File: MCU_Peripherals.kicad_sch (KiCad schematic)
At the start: 17 parts

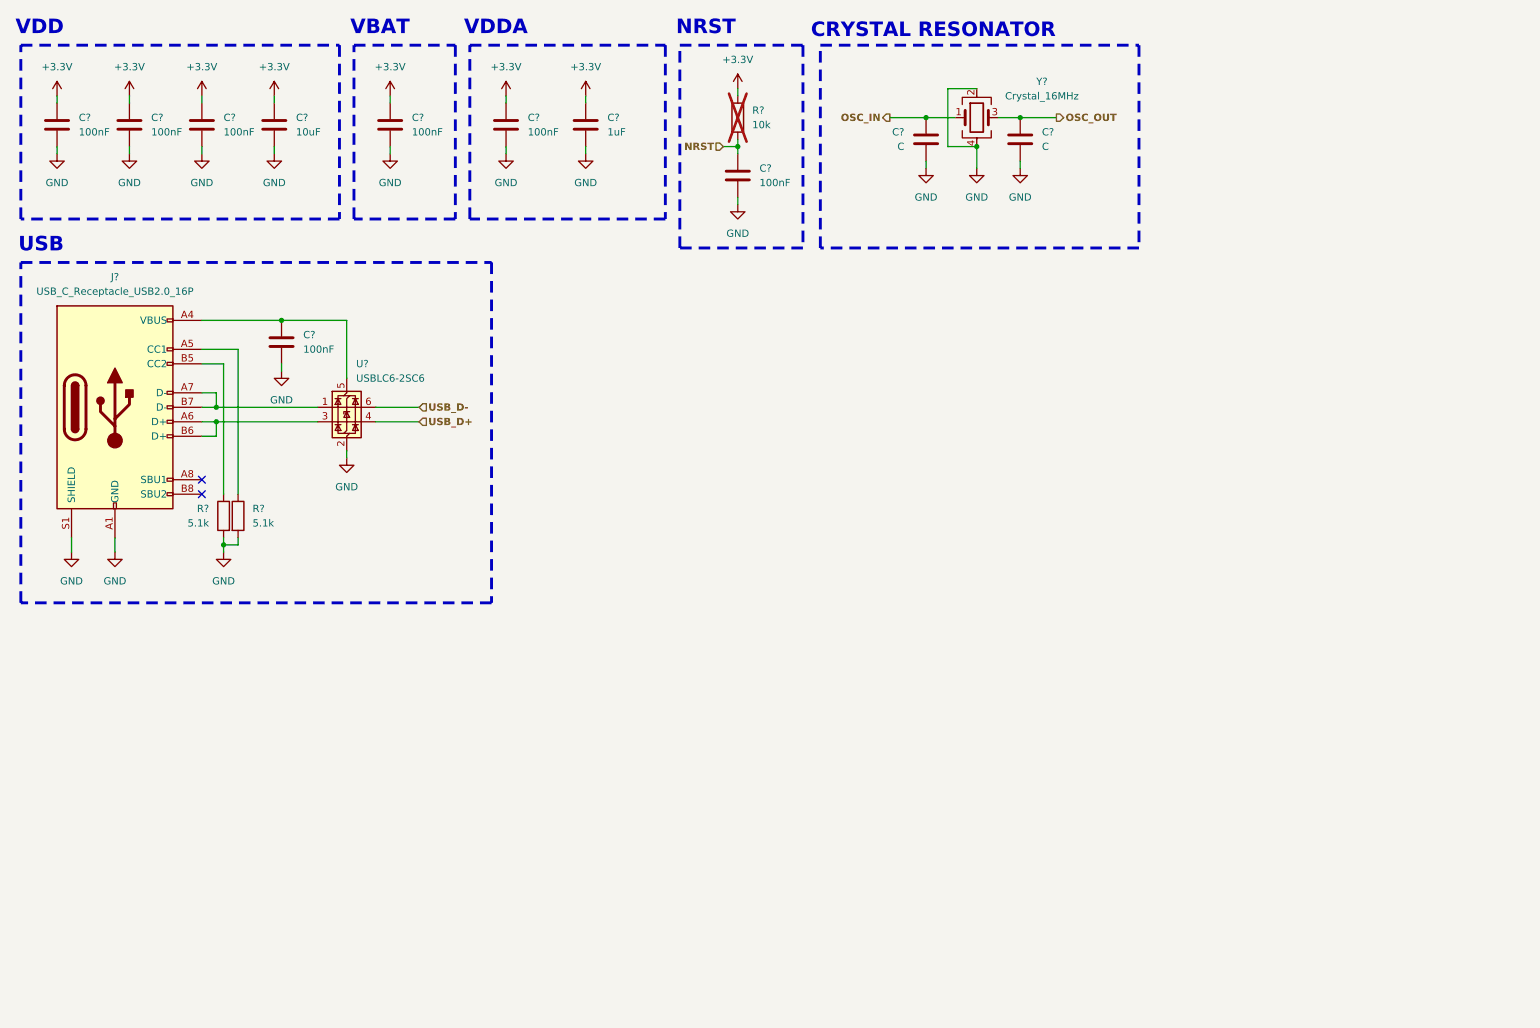
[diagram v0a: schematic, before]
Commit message: Power Rail Update
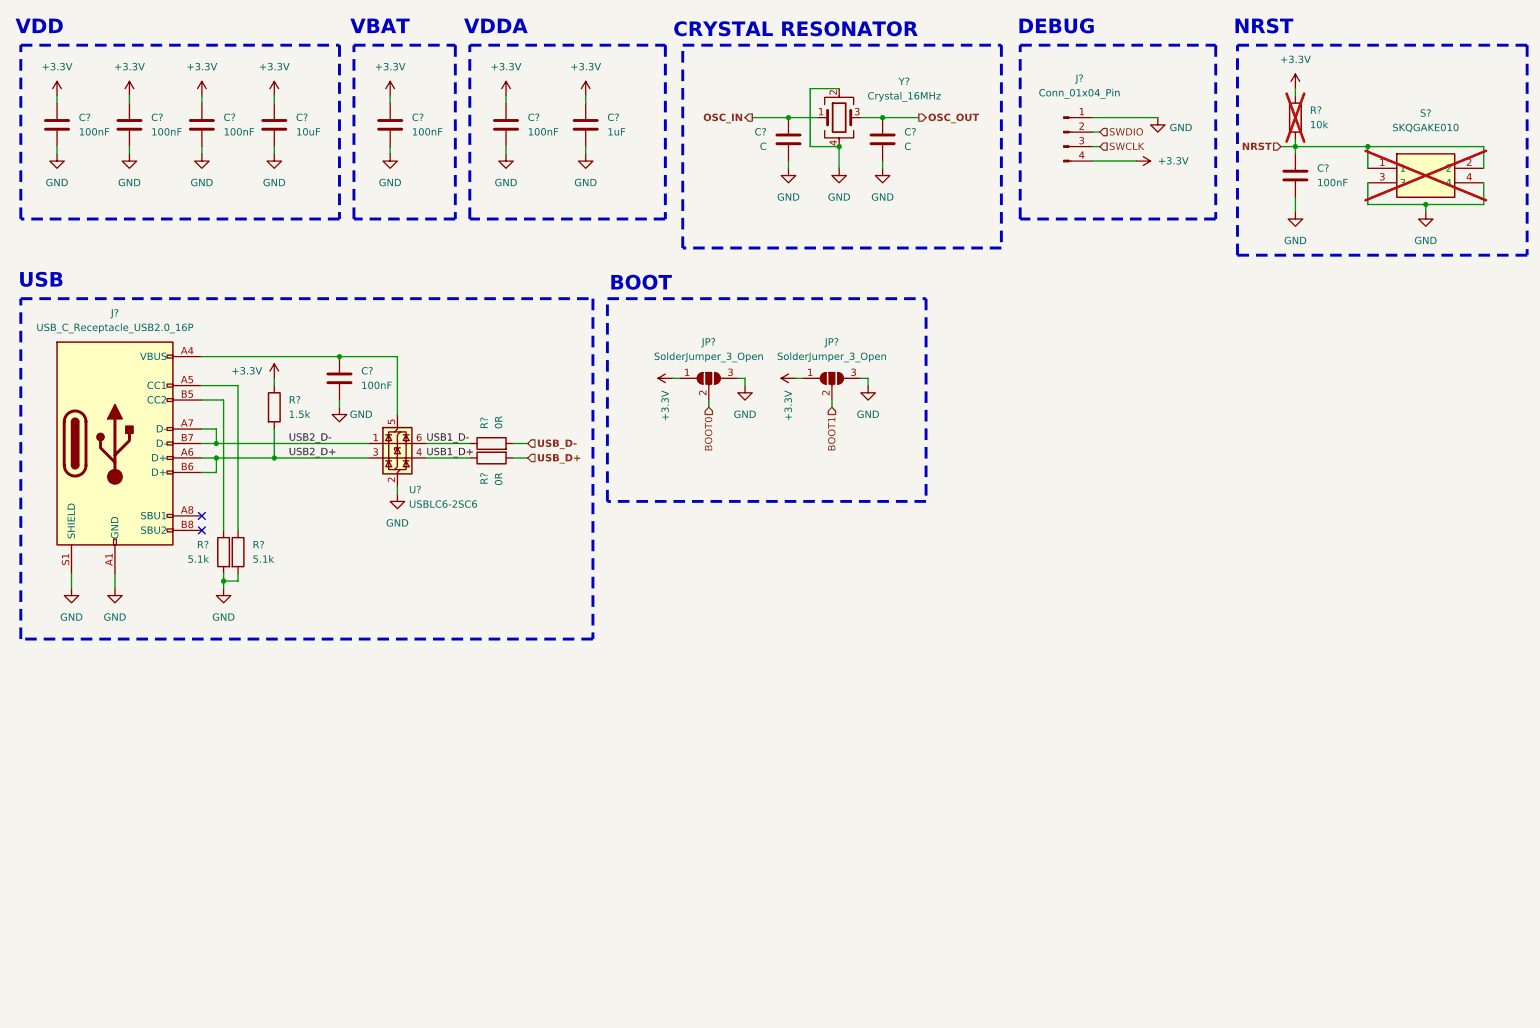
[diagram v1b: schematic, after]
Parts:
- added J?: Conn_01x04_Pin, symbol Connector:Conn_01x04_Pin
- added JP? (x2): SolderJumper_3_Open, symbol Jumper:SolderJumper_3_Open
- added R? (x2): 0R, symbol Device:R
- added R?: 1.5k, symbol Device:R
- added S?: SKQGAKE010, KSZ_KiCad_Footprint_Library:SKQGAKE010, symbol KSZ_KiCad_Symbol_Library:SKQGAKE010
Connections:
- net +3.3V: now also J?.4 (Pin_4), JP?.1 (A), JP?.1 (A), R?.1
- net GND: now also J?.1 (Pin_1), JP?.3 (B), JP?.3 (B), S?.3, S?.4
- net NRST: now also S?.1, S?.2
- net USB_D+: now also R?.2; no longer U?.4 (I/O2)
- net USB_D-: now also R?.2; no longer U?.6 (I/O1)
- net USB2_D+: now reaches J?.A6 (D+), J?.B6 (D+), U?.3 (I/O2)
- net USB2_D+: now also R?.2
- net USB2_D-: now reaches J?.A7 (D-), J?.B7 (D-), U?.1 (I/O1)
- new net BOOT0: JP?.2 (C)
- new net BOOT1: JP?.2 (C)
- new net SWCLK: J?.3 (Pin_3)
- new net SWDIO: J?.2 (Pin_2)
- new net USB1_D+: R?.1, U?.4 (I/O2)
- new net USB1_D-: R?.1, U?.6 (I/O1)
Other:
- note added: "BOOT"
- note added: "DEBUG"
- moved on the sheet: C?, J?, R?, U?, Y?

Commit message: Stepper Motor Control Update
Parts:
- added R? (x2): 4.7k, symbol Device:R
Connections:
- net +3.3V: now also R?.1, R?.1
- new net SCL: R?.2
- new net SDA: R?.2
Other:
- note added: "I2C"

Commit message: CAN & EEPROM Update
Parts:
- added C? (x2): 100nF, symbol Device:C
- added D?: PESD2CANFD24V-UX, KSZ_KiCad_Footprint_Library:TVS_PESD2CANFD24V-UX, symbol KSZ_KiCad_Symbol_Library:PESD2CANFD24V-UX
- added J?: Conn_01x02_Socket, symbol Connector:Conn_01x02_Socket
- added JP? (x3): SolderJumper_3_Open, symbol Jumper:SolderJumper_3_Open
- added R?: 120R, symbol Device:R
- added R?: 10k, symbol Device:R
- added U?: SN65HVD230DR, KSZ_KiCad_Footprint_Library:SOIC127P599X175-8N, symbol KSZ_KiCad_Symbol_Library:SN65HVD230DR
- added U?: M24C64-RMN6TP, KSZ_KiCad_Footprint_Library:SOIC127P600X175-8N, symbol KSZ_KiCad_Symbol_Library:M24C64-RMN6TP
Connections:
- net +3.3V: now also C?.1, C?.1, JP?.1 (A), JP?.1 (A), JP?.1 (A), U?.3 (VCC), U?.8 (VCC)
- net GND: now also C?.2, C?.2, D?.3, JP?.3 (B), JP?.3 (B), JP?.3 (B), R?.2, U?.2 (GND), U?.4 (VSS)
- new net: D?.1, J?.2 (Pin_2), R?.2, U?.6 (CANL)
- new net: D?.2, J?.1 (Pin_1), R?.1, U?.7 (CANH)
- new net: R?.1, U?.8 (RS)
- new net CAN_RX: U?.4 (R)
- new net CAN_TX: U?.1 (D)
- new net E0: JP?.2 (C), U?.1 (E0)
- new net E1: JP?.2 (C), U?.2 (E1)
- new net E2: JP?.2 (C), U?.3 (E2)
- new net SCL_EEPROM: U?.6 (SCL)
- new net SDA_EEPROM: U?.5 (SDA)
- new net WC_EEPROM: U?.7 (~{WC})
- no-connect marks 2 -> 3
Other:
- note added: "CAN"
- note added: "EEPROM"

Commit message: LEDs, Button & Small fixes
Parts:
- added D?: R_LED, symbol Device:LED
- added D?: B_LED, symbol Device:LED
- added D?: G_LED, symbol Device:LED
- added R? (x3): 1.5k, symbol Device:R
- added R?: 10k, symbol Device:R
- added S?: SKQGAKE010, KSZ_KiCad_Footprint_Library:SKQGAKE010, symbol KSZ_KiCad_Symbol_Library:SKQGAKE010
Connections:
- net +3.3V: now also D?.2 (A), D?.2 (A), D?.2 (A), R?.1
- net GND: now also S?.3, S?.4
- new net: D?.1 (K), R?.1 (x3)
- new net B_LED: R?.2
- new net G_LED: R?.2
- new net R_LED: R?.2
- new net U_BUTTON: R?.2, S?.1, S?.2
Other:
- note added: "STATE_LEDS"
- note added: "USER_BUTTON"

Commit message: Schematic finish & ERC
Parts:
- gave numbers to parts that had none: 45

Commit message: Footprint Update
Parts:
- C1, C10, C11, C12, C13, C2, C3, C4, C5, C6, C7, C8, C9: footprint (none) -> Capacitor_SMD:C_0402_1005Metric_Pad0.74x0.62mm_HandSolder
- D2, D3, D4: footprint (none) -> LED_SMD:LED_0603_1608Metric_Pad1.05x0.95mm_HandSolder
- J1: footprint (none) -> Connector_USB:USB_C_Receptacle_HRO_TYPE-C-31-M-12
- J2: footprint (none) -> TerminalBlock:TerminalBlock_MaiXu_MX126-5.0-02P_1x02_P5.00mm
- J3: footprint (none) -> Connector_PinHeader_2.54mm:PinHeader_1x04_P2.54mm_Vertical
- JP1, JP2, JP3, JP4, JP5: footprint (none) -> Jumper:SolderJumper-3_P1.3mm_Open_RoundedPad1.0x1.5mm_NumberLabels
- R1, R10, R11, R12, R13, R14, R2, R3, R4, R5, R6, R7, R8, R9: footprint (none) -> Resistor_SMD:R_0402_1005Metric_Pad0.72x0.64mm_HandSolder
- Y1: footprint (none) -> Crystal:Crystal_SMD_3225-4Pin_3.2x2.5mm_HandSoldering
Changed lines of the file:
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@@
 			)
 		)
-		(property "Footprint" ""
+		(property "Footprint" "Jumper:SolderJumper-3_P1.3mm_Open_RoundedPad1.0x1.5mm_NumberLabels"
 			(at 208.28 115.57 0)
 			(effects
@@
 			)
 		)
-		(property "Footprint" ""
+		(property "Footprint" "Capacitor_SMD:C_0402_1005Metric_Pad0.74x0.62mm_HandSolder"
 			(at 72.0852 81.28 0)
 			(effects
@@
 			)
 		)
-		(property "Footprint" ""
+		(property "Footprint" "Resistor_SMD:R_0402_1005Metric_Pad0.72x0.64mm_HandSolder"
 			(at 51.562 107.95 90)
 			(effects
@@
 			)
 		)
-		(property "Footprint" ""
+		(property "Footprint" "Capacitor_SMD:C_0402_1005Metric_Pad0.74x0.62mm_HandSolder"
 			(at 167.3352 39.37 0)
 			(effects
@@
 			)
 		)
-		(property "Footprint" ""
+		(property "Footprint" "Capacitor_SMD:C_0402_1005Metric_Pad0.74x0.62mm_HandSolder"
 			(at 115.2652 36.83 0)
 			(effects
@@
 			)
 		)
-		(property "Footprint" ""
+		(property "Footprint" "Resistor_SMD:R_0402_1005Metric_Pad0.72x0.64mm_HandSolder"
 			(at 97.79 89.662 90)
 			(effects
@@
 			)
 		)
-		(property "Footprint" ""
+		(property "Footprint" "LED_SMD:LED_0603_1608Metric_Pad1.05x0.95mm_HandSolder"
 			(at 128.27 163.83 0)
 			(effects
@@
 			)
 		)
-		(property "Footprint" ""
+		(property "Footprint" "Jumper:SolderJumper-3_P1.3mm_Open_RoundedPad1.0x1.5mm_NumberLabels"
 			(at 208.28 129.54 0)
 			(effects
@@
 			)
 		)
-		(property "Footprint" ""
+		(property "Footprint" "Jumper:SolderJumper-3_P1.3mm_Open_RoundedPad1.0x1.5mm_NumberLabels"
 			(at 135.89 77.47 0)
 			(effects
@@
 			)
 		)
-		(property "Footprint" ""
+		(property "Footprint" "Capacitor_SMD:C_0402_1005Metric_Pad0.74x0.62mm_HandSolder"
 			(at 47.9552 36.83 0)
 			(effects
@@
 			)
 		)
-		(property "Footprint" ""
+		(property "Footprint" "Resistor_SMD:R_0402_1005Metric_Pad0.72x0.64mm_HandSolder"
 			(at 52.578 107.95 90)
 			(effects
@@
 			)
 		)
-		(property "Footprint" ""
+		(property "Footprint" "Capacitor_SMD:C_0402_1005Metric_Pad0.74x0.62mm_HandSolder"
 			(at 101.2952 36.83 0)
 			(effects
@@
 			)
 		)
-		(property "Footprint" ""
+		(property "Footprint" "Jumper:SolderJumper-3_P1.3mm_Open_RoundedPad1.0x1.5mm_NumberLabels"
 			(at 241.3 115.57 0)
 			(effects
@@
 			)
 		)
-		(property "Footprint" ""
+		(property "Footprint" "LED_SMD:LED_0603_1608Metric_Pad1.05x0.95mm_HandSolder"
 			(at 139.7 163.83 0)
 			(effects
@@
 			)
 		)
-		(property "Footprint" ""
+		(property "Footprint" "Connector_PinHeader_2.54mm:PinHeader_1x04_P2.54mm_Vertical"
 			(at 198.12 34.29 0)
 			(effects
@@
 			)
 		)
-		(property "Footprint" ""
+		(property "Footprint" "Resistor_SMD:R_0402_1005Metric_Pad0.72x0.64mm_HandSolder"
 			(at 195.072 74.93 90)
 			(effects
@@
 			)
 		)
-		(property "Footprint" ""
+		(property "Footprint" "Capacitor_SMD:C_0402_1005Metric_Pad0.74x0.62mm_HandSolder"
 			(at 239.7252 45.72 0)
 			(effects
@@
 			)
 		)
-		(property "Footprint" ""
+		(property "Footprint" "Resistor_SMD:R_0402_1005Metric_Pad0.72x0.64mm_HandSolder"
 			(at 83.312 149.86 90)
 			(effects
@@
 			)
 		)
-		(property "Footprint" ""
+		(property "Footprint" "Jumper:SolderJumper-3_P1.3mm_Open_RoundedPad1.0x1.5mm_NumberLabels"
 			(at 157.48 77.47 0)
 			(effects
@@
 			)
 		)
-		(property "Footprint" ""
+		(property "Footprint" "Resistor_SMD:R_0402_1005Metric_Pad0.72x0.64mm_HandSolder"
 			(at 57.912 82.55 90)
 			(effects
@@
 			)
 		)
-		(property "Footprint" ""
+		(property "Footprint" "Connector_USB:USB_C_Receptacle_HRO_TYPE-C-31-M-12"
 			(at 35.56 88.9 0)
 			(effects
@@
 			)
 		)
-		(property "Footprint" ""
+		(property "Footprint" "Resistor_SMD:R_0402_1005Metric_Pad0.72x0.64mm_HandSolder"
 			(at 203.962 74.93 90)
 			(effects
@@
 			)
 		)
-		(property "Footprint" ""
+		(property "Footprint" "Capacitor_SMD:C_0402_1005Metric_Pad0.74x0.62mm_HandSolder"
 			(at 177.8 117.1448 0)
 			(effects
@@
 			)
 		)
-		(property "Footprint" ""
+		(property "Footprint" "Resistor_SMD:R_0402_1005Metric_Pad0.72x0.64mm_HandSolder"
 			(at 97.79 90.678 90)
 			(effects
@@
 			)
 		)
-		(property "Footprint" ""
+		(property "Footprint" "Capacitor_SMD:C_0402_1005Metric_Pad0.74x0.62mm_HandSolder"
 			(at 60.6552 36.83 0)
 			(effects
@@
 			)
 		)
-		(property "Footprint" ""
+		(property "Footprint" "Resistor_SMD:R_0402_1005Metric_Pad0.72x0.64mm_HandSolder"
 			(at 130.048 172.72 90)
 			(effects
@@
 			)
 		)
-		(property "Footprint" ""
+		(property "Footprint" "Capacitor_SMD:C_0402_1005Metric_Pad0.74x0.62mm_HandSolder"
 			(at 148.8948 39.37 0)
 			(effects
@@
 			)
 		)
-		(property "Footprint" ""
+		(property "Footprint" "Resistor_SMD:R_0402_1005Metric_Pad0.72x0.64mm_HandSolder"
 			(at 236.982 76.2 90)
 			(effects
@@
 			)
 		)
-		(property "Footprint" ""
+		(property "Footprint" "Resistor_SMD:R_0402_1005Metric_Pad0.72x0.64mm_HandSolder"
 			(at 141.478 172.72 90)
 			(effects
@@
 			)
 		)
-		(property "Footprint" ""
+		(property "Footprint" "Capacitor_SMD:C_0402_1005Metric_Pad0.74x0.62mm_HandSolder"
 			(at 22.5552 36.83 0)
 			(effects
@@
 			)
 		)
-		(property "Footprint" ""
+		(property "Footprint" "LED_SMD:LED_0603_1608Metric_Pad1.05x0.95mm_HandSolder"
 			(at 151.13 163.83 0)
 			(effects
@@
 			)
 		)
-		(property "Footprint" ""
+		(property "Footprint" "Capacitor_SMD:C_0402_1005Metric_Pad0.74x0.62mm_HandSolder"
 			(at 35.2552 36.83 0)
 			(effects
@@
 			)
 		)
-		(property "Footprint" ""
+		(property "Footprint" "TerminalBlock:TerminalBlock_MaiXu_MX126-5.0-02P_1x02_P5.00mm"
 			(at 104.14 148.59 0)
 			(effects
@@
 			)
 		)
-		(property "Footprint" ""
+		(property "Footprint" "Resistor_SMD:R_0402_1005Metric_Pad0.72x0.64mm_HandSolder"
 			(at 30.988 156.21 90)
 			(effects
@@
 			)
 		)
-		(property "Footprint" ""
+		(property "Footprint" "Capacitor_SMD:C_0402_1005Metric_Pad0.74x0.62mm_HandSolder"
 			(at 80.9752 36.83 0)
 			(effects
@@
 			)
 		)
-		(property "Footprint" ""
+		(property "Footprint" "Resistor_SMD:R_0402_1005Metric_Pad0.72x0.64mm_HandSolder"
 			(at 236.982 31.75 90)
 			(effects
@@
 			)
 		)
-		(property "Footprint" ""
+		(property "Footprint" "Resistor_SMD:R_0402_1005Metric_Pad0.72x0.64mm_HandSolder"
 			(at 152.908 172.72 90)
 			(effects
@@
 			)
 		)
-		(property "Footprint" ""
+		(property "Footprint" "Capacitor_SMD:C_0402_1005Metric_Pad0.74x0.62mm_HandSolder"
 			(at 78.74 142.5448 0)
 			(effects
@@
 			)
 		)
-		(property "Footprint" ""
+		(property "Footprint" "Crystal:Crystal_SMD_3225-4Pin_3.2x2.5mm_HandSoldering"
 			(at 158.75 31.75 0)
 			(effects

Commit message: Layout Update
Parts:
- removed C4: 10uF, Capacitor_SMD:C_0402_1005Metric_Pad0.74x0.62mm_HandSolder, symbol Device:C
- removed JP1, JP2, JP3, JP4, JP5: SolderJumper_3_Open, Jumper:SolderJumper-3_P1.3mm_Open_RoundedPad1.0x1.5mm_NumberLabels, symbol Jumper:SolderJumper_3_Open
- removed R13: 10k, Resistor_SMD:R_0402_1005Metric_Pad0.72x0.64mm_HandSolder, symbol Device:R
- removed R6, R7: 0R, Resistor_SMD:R_0402_1005Metric_Pad0.72x0.64mm_HandSolder, symbol Device:R
- removed S1, S2: SKQGAKE010, KSZ_KiCad_Footprint_Library:SKQGAKE010, symbol KSZ_KiCad_Symbol_Library:SKQGAKE010
- added J6: Conn_01x02_Socket, Connector_JST:JST_PH_S2B-PH-K_1x02_P2.00mm_Horizontal, symbol Connector:Conn_01x02_Socket
- added S1: SKRPABE010, KSZ_KiCad_Footprint_Library:SW_SKRPABE010, symbol KSZ_KiCad_Symbol_Library:SKRPABE010
- J2: footprint TerminalBlock:TerminalBlock_MaiXu_MX126-5.0-02P_1x02_P5.00mm -> Connector_JST:JST_PH_S2B-PH-K_1x02_P2.00mm_Horizontal
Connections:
- net E0 is gone; now on net GND: U4.1 (E0)
- net E1 is gone; now on net GND: U4.2 (E1)
- net E2 is gone; now on net GND: U4.3 (E2)
- net USB1_D+ is gone; now on net USB_D+: U3.4 (I/O2)
- net USB1_D- is gone; now on net USB_D-: U3.6 (I/O1)
- net GND: now also S1.3, S1.4
- net U_BUTTON: now also S1.1, S1.2
- net CANL: now reaches D1.1, R5.2, U2.6 (CANL)
- net CANL: now also J2.1 (Pin_1), J6.1 (Pin_1); no longer J2.2 (Pin_2)
- net CANH: now reaches D1.2, R5.1, U2.7 (CANH)
- net CANH: now also J2.2 (Pin_2), J6.2 (Pin_2); no longer J2.1 (Pin_1)
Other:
- note removed: "BOOT"
- moved on the sheet: C12, C13, D2, D3, D4, R10, R5, R8, R9, U4

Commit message: Layout Update
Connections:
- net CANH renamed CAN_P
- net CANL renamed CAN_N
- net CAN_N: no longer J6.1 (Pin_1), R5.2
- new net CANL_N: J6.1 (Pin_1), R5.2
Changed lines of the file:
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@@
 		)
 	)
-	(label "CANH"
+	(label "CAN_P"
 		(at 99.06 146.05 0)
 		(effects
@@
 		)
 	)
-	(label "CANL"
+	(label "CANL_N"
 		(at 128.27 173.99 0)
 		(effects
@@
 		)
 	)
-	(label "CANL"
+	(label "CAN_N"
 		(at 99.06 153.67 0)
 		(effects
@@
 		)
 	)
-	(label "CANH"
+	(label "CAN_P"
 		(at 128.27 166.37 0)
 		(effects
